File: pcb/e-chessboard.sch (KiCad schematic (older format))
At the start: 58 parts

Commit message: feat(kicad): adding ldr sensors
Adding ldr sensors to the matrix for checking the location of the chess
pieces.
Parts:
- removed D? (x9): D, Diode_SMD:D_SMA, symbol Device:D
- removed J?: e-magnet-2, lib_fp:20_15_electromagnet, symbol Connector:Conn_01x02_Male
- removed J?: e-magnet-5, lib_fp:20_15_electromagnet, symbol Connector:Conn_01x02_Male
- removed J?: e-magnet-8, lib_fp:20_15_electromagnet, symbol Connector:Conn_01x02_Male
- removed J?: e-magnet-4, lib_fp:20_15_electromagnet, symbol Connector:Conn_01x02_Male
- removed J?: e-magnet-1, lib_fp:20_15_electromagnet, symbol Connector:Conn_01x02_Male
- removed J?: e-magnet-3, lib_fp:20_15_electromagnet, symbol Connector:Conn_01x02_Male
- removed J?: e-magnet-7, lib_fp:20_15_electromagnet, symbol Connector:Conn_01x02_Male
- removed J?: e-magnet-6, lib_fp:20_15_electromagnet, symbol Connector:Conn_01x02_Male
- removed J?: e-magnet-9, lib_fp:20_15_electromagnet, symbol Connector:Conn_01x02_Male
- removed R? (x4): 100k, Resistor_SMD:R_0805_2012Metric, symbol Device:R
- added C?: 100nF, Capacitor_SMD:C_0805_2012Metric_Pad1.15x1.40mm_HandSolder, symbol Device:C
- added C?: 100n, Capacitor_SMD:C_0805_2012Metric_Pad1.15x1.40mm_HandSolder, symbol Device:C
- added D? (x9): D, Diode_SMD:D_SMA, symbol Device:D
- added D? (x6): D_Zener, Diode_SMD:D_SOD-110, symbol Device:D_Zener
- added R? (x3): 10k, Resistor_SMD:R_0805_2012Metric, symbol Device:R
- added U? (x9): MAGNET_LDR, lib_fp:20_15_electromagnet_ldr, symbol lib:MAGNET_LDR
- added U?: NCV7608, Package_SO:SOIC-28W_7.5x17.9mm_P1.27mm, symbol lib:NCV7608
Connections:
- net +12V: now also C?.2, U?.1 (D2), U?.24 (VS), U?.28 (D3), U?.4 (D1)
- net +3V3: now also C?.2, D?.1 (K), D?.1 (K), D?.1 (K), U?.8 (VCC)
- net GND: now also C?.1, C?.1, D?.2 (A), D?.2 (A), D?.2 (A), U?.10 (GND), U?.4, U?.4, U?.4, U?.4, U?.4, U?.4, U?.4, U?.4, U?.4
- net LDR_CS: now reaches U?.28 (IO17)
- net LDR_CS: now also U?.5 (CSB)
- net MAG_EN: now reaches U?.30 (IO18)
- net MAG_EN: now also U?.19 (EN)
- net LDR_EN: now reaches U?.31 (IO19)
- net LDR_EN: now also U?.19 (EN)
- net LDR_ADC3: now reaches U?.4 (SENSOR_VP)
- net LDR_ADC3: now also D?.1 (K), D?.2 (A), R?.2, U?.3, U?.3, U?.3
- net LDR_ADC1: now reaches U?.6 (IO34)
- net LDR_ADC1: now also D?.1 (K), D?.2 (A), R?.2, U?.3, U?.3, U?.3
- net LDR_ADC2: now reaches U?.7 (IO35)
- net LDR_ADC2: now also D?.1 (K), D?.2 (A), R?.2, U?.3, U?.3, U?.3
- net COL_1 renamed MAG_COL_1
- net MAG_COL_1: now also D?.1 (K), D?.1 (K), D?.1 (K), U?.2, U?.2, U?.2
- net COL_2 renamed MAG_COL_2
- net MAG_COL_2: now also D?.1 (K), D?.1 (K), D?.1 (K), U?.2, U?.2, U?.2
- net EN_MAG renamed MAG_CS
- net MAG_CS: now also U?.5 (CSB); no longer U?.19 (EN)
- net MISO_MAG renamed MISO
- net MISO: now also U?.9 (SO)
- net MOSI_MAG renamed MOSI
- net MOSI: now also U?.7 (SI)
- net PWM_ROW1 renamed MAG_PWM_ROW1
- net PWM_ROW2 renamed MAG_PWM_ROW2
- net PWM_ROW3 renamed MAG_PWM_ROW3
- net ROW_1 renamed MAG_ROW_1
- net MAG_ROW_1: now also D?.2 (A), D?.2 (A), D?.2 (A), U?.1, U?.1, U?.1
- net ROW_2 renamed MAG_ROW_2
- net MAG_ROW_2: now also D?.2 (A), D?.2 (A), D?.2 (A), U?.1, U?.1, U?.1
- net ROW_3 renamed MAG_ROW_3
- net MAG_ROW_3: now also D?.2 (A), D?.2 (A), D?.2 (A), U?.1, U?.1, U?.1
- net SCLK_MAG renamed SCLK
- net SCLK: now also U?.6 (SCLK)
- net SS_MAG: no longer names the net of U?.23 (IO15)
- net SS_MAG: no longer U?.5 (CSB)
- new net LDR_ROW1: R?.1, U?.3 (S1)
- new net LDR_ROW2: R?.1, U?.2 (S2)
- new net LDR_ROW3: R?.1, U?.27 (S3)
- new net MAG_COL_3: D?.1 (K), D?.1 (K), D?.1 (K), U?.2, U?.2, U?.2
- no-connect marks 30 -> 39
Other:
- moved on the sheet: C?, H?, J?, Q?, R?, SW?, U?

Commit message: feat(kicad): generating netlist
Fixing all erc issues, adding power and fuse footprints and generating
netlist.
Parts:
- F1: renamed from F?; footprint (none) -> Fuse:Fuseholder_Cylinder-5x20mm_Schurter_0031_8201_Horizontal_Open
- J1: renamed from J?; footprint (none) -> Connector_BarrelJack:BarrelJack_CUI_PJ-102AH_Horizontal
- gave numbers to parts that had none: 64
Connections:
- net COL_3 is gone; now on net MAG_COL_3: U3.27 (S3)
- net +3V3: now also C8.1, L1.2, R3.1

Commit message: fix(kicad): adding more traces
Adding traces and changing some schematic outputs for optimization.
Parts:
- R7, R8, R9: value 10k -> 300k
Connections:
- net LDR_ADC1: now also D1.2 (A), D2.1 (K), U1.4 (SENSOR_VP); no longer D6.2 (A), D7.1 (K), U1.6 (IO34)
- net LDR_ADC2: now also D6.2 (A), D7.1 (K), U1.6 (IO34); no longer D4.2 (A), D5.1 (K), U1.7 (IO35)
- net LDR_ADC3: now also D4.2 (A), D5.1 (K), U1.7 (IO35); no longer D1.2 (A), D2.1 (K), U1.4 (SENSOR_VP)
- net MAG_COL_1: now also D15.1 (K), D16.1 (K), D17.1 (K), U10.2, U11.2, U12.2; no longer D10.1 (K), D11.1 (K), D9.1 (K), U4.2, U5.2, U6.2
- net MAG_COL_3: now also D10.1 (K), D11.1 (K), D9.1 (K), U4.2, U5.2, U6.2; no longer D15.1 (K), D16.1 (K), D17.1 (K), U10.2, U11.2, U12.2
- net MAG_PWM_ROW1: now also U1.8 (IO32); no longer U1.12 (IO27)
- net MAG_PWM_ROW2: now also U1.9 (IO33); no longer U1.8 (IO32)
- net MAG_PWM_ROW3: now also U1.12 (IO27); no longer U1.9 (IO33)
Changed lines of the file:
@@
 Text GLabel 12750 4950 1    50   Input ~ 0
 MAG_COL_2
-Text GLabel 13750 4950 1    50   Input ~ 0
+Text GLabel 11750 5000 1    50   Input ~ 0
 MAG_COL_3
 $Comp
@@
 Text GLabel 9600 2150 2    50   Input ~ 0
 MAG_PWM_ROW3
+Text GLabel 2800 6500 2    50   Output ~ 0
+MAG_PWM_ROW1
+Text GLabel 2800 6600 2    50   Output ~ 0
+MAG_PWM_ROW2
 Text GLabel 2800 6400 2    50   Output ~ 0
-MAG_PWM_ROW1
-Text GLabel 2800 6500 2    50   Output ~ 0
-MAG_PWM_ROW2
-Text GLabel 2800 6600 2    50   Output ~ 0
 MAG_PWM_ROW3
 Text GLabel 9600 2450 2    50   Input ~ 0
@@
 Wire Wire Line
 	11750 5750 11600 5750
-Text GLabel 11750 5000 1    50   Input ~ 0
+Text GLabel 13750 4950 1    50   Input ~ 0
 MAG_COL_1
 Wire Wire Line
@@
 P 10350 5200
 F 0 "R7" V 10450 5150 50  0000 L CNN
-F 1 "10k" V 10350 5150 50  0000 L CNN
+F 1 "300k" V 10350 5100 50  0000 L CNN
 F 2 "Resistor_SMD:R_0805_2012Metric" V 10280 5200 50  0001 C CNN
 F 3 "~" H 10350 5200 50  0001 C CNN
@@
 P 10350 6200
 F 0 "R8" V 10450 6150 50  0000 L CNN
-F 1 "10k" V 10350 6150 50  0000 L CNN
+F 1 "300k" V 10350 6100 50  0000 L CNN
 F 2 "Resistor_SMD:R_0805_2012Metric" V 10280 6200 50  0001 C CNN
 F 3 "~" H 10350 6200 50  0001 C CNN
@@
 P 10350 7200
 F 0 "R9" V 10450 7150 50  0000 L CNN
-F 1 "10k" V 10350 7100 50  0000 L CNN
+F 1 "300k" V 10350 7100 50  0000 L CNN
 F 2 "Resistor_SMD:R_0805_2012Metric" V 10280 7200 50  0001 C CNN
 F 3 "~" H 10350 7200 50  0001 C CNN
@@
 Wire Wire Line
 	10550 5200 10550 5350
+Text GLabel 1050 4700 0    50   Input ~ 0
+LDR_ADC1
 Text GLabel 3500 7600 3    50   Input ~ 0
-LDR_ADC1
+LDR_ADC2
 Text GLabel 2800 7600 3    50   Input ~ 0
-LDR_ADC2
-Text GLabel 1050 4700 0    50   Input ~ 0
 LDR_ADC3
 $Comp

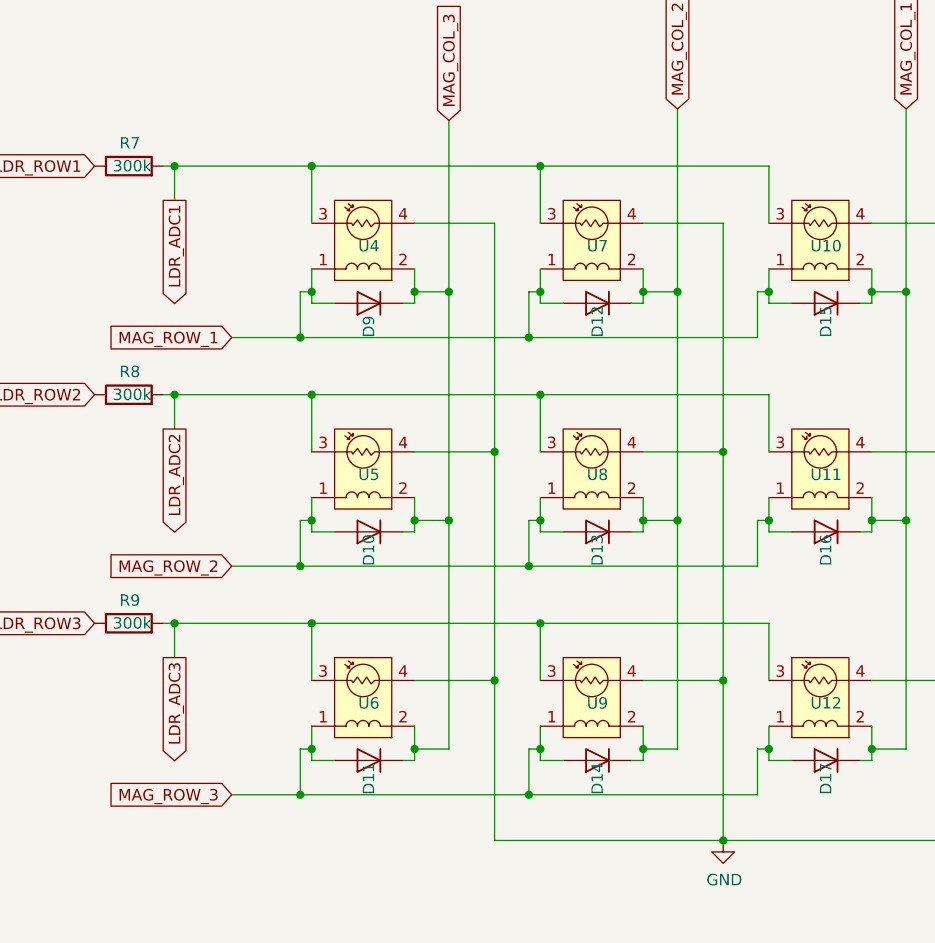
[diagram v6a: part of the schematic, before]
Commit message: fix(kicad): fixing wrong ldr lineup in the matrix
Fixing issue #2. Pcb not updated yet.
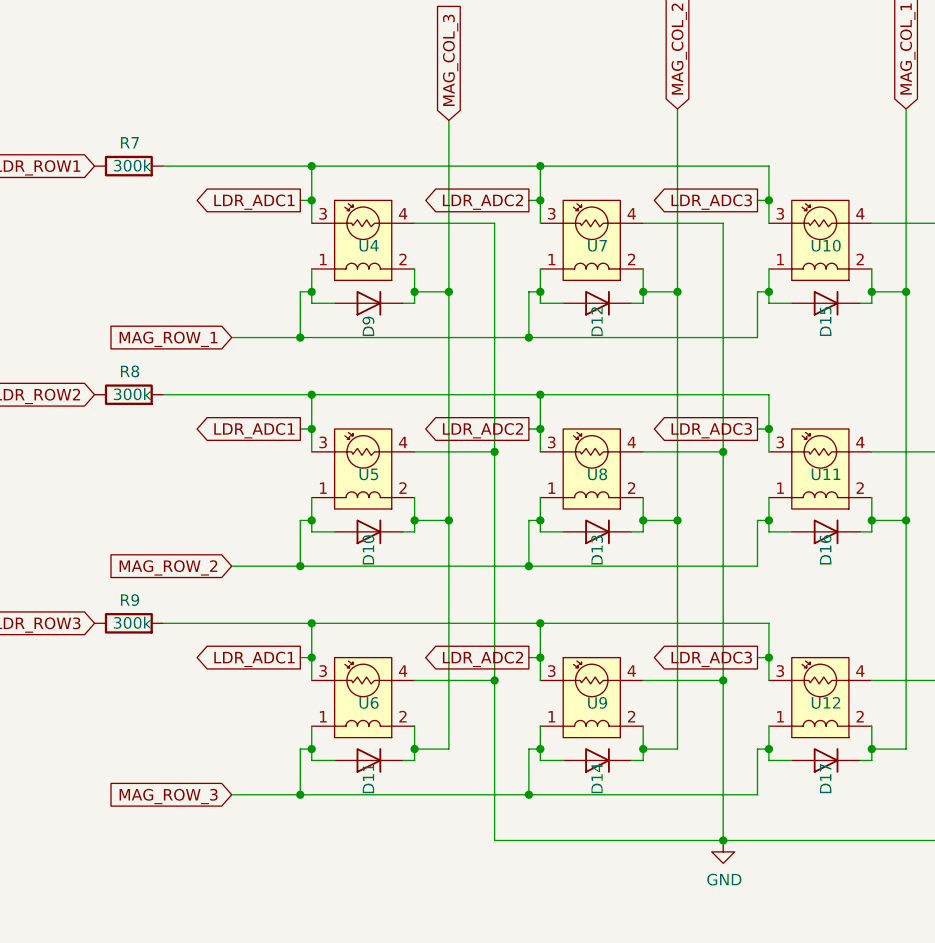
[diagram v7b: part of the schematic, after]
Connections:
- net LDR_ADC2 is gone; now on net LDR_ADC1: D6.2 (A), D7.1 (K), R8.2, U1.6 (IO34), U11.3, U5.3, U8.3
- net LDR_ADC3 is gone; now on net LDR_ADC1: D4.2 (A), D5.1 (K), R9.2, U1.7 (IO35), U12.3, U6.3, U9.3
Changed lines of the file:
@@
 LDR_ROW1
 Wire Wire Line
-	13150 5200 13150 5450
-Wire Wire Line
-	12150 5450 12150 5200
+	13150 5200 13150 5350
+Wire Wire Line
+	12150 5450 12150 5350
 Connection ~ 12150 5200
 Wire Wire Line
 	12150 5200 13150 5200
 Wire Wire Line
-	11150 5450 11150 5200
+	11150 5450 11150 5350
 Wire Wire Line
 	11150 5200 12150 5200
 Wire Wire Line
-	13150 6200 13150 6450
-Wire Wire Line
-	12150 6450 12150 6200
+	13150 6200 13150 6350
+Wire Wire Line
+	12150 6450 12150 6350
 Connection ~ 12150 6200
 Wire Wire Line
 	12150 6200 13150 6200
 Wire Wire Line
-	11150 6450 11150 6200
+	11150 6450 11150 6350
 Wire Wire Line
 	11150 6200 12150 6200
 Wire Wire Line
-	13150 7200 13150 7450
-Wire Wire Line
-	12150 7450 12150 7200
+	13150 7200 13150 7350
+Wire Wire Line
+	12150 7450 12150 7350
 Connection ~ 12150 7200
 Wire Wire Line
 	12150 7200 13150 7200
 Wire Wire Line
-	11150 7450 11150 7200
+	11150 7450 11150 7350
 Wire Wire Line
 	11150 7200 12150 7200
@@
 Wire Wire Line
 	12950 8150 13950 8150
-Text GLabel 10550 5350 3    50   Output ~ 0
+Text GLabel 11100 5350 0    50   Output ~ 0
 LDR_ADC1
-Text GLabel 10550 6350 3    50   Output ~ 0
+Text GLabel 12100 5350 0    50   Output ~ 0
 LDR_ADC2
-Text GLabel 10550 7350 3    50   Output ~ 0
+Text GLabel 13100 5350 0    50   Output ~ 0
 LDR_ADC3
 $Comp
@@
 	11750 5000 11750 5750
 Connection ~ 11750 5750
-Wire Wire Line
-	10500 5200 10550 5200
 Connection ~ 11150 5200
-Connection ~ 10550 5200
-Wire Wire Line
-	10550 5200 11150 5200
-Wire Wire Line
-	10500 6200 10550 6200
-Wire Wire Line
-	10550 6200 10550 6350
-Wire Wire Line
-	10550 6200 11150 6200
-Connection ~ 10550 6200
 Connection ~ 11150 6200
-Wire Wire Line
-	10500 7200 10550 7200
-Wire Wire Line
-	10550 7200 10550 7350
-Wire Wire Line
-	10550 7200 11150 7200
-Connection ~ 10550 7200
 Connection ~ 11150 7200
-Wire Wire Line
-	10550 5200 10550 5350
 Text GLabel 1050 4700 0    50   Input ~ 0
 LDR_ADC1
@@
 	0    1    1    0
 $EndComp
+Wire Wire Line
+	10500 5200 11150 5200
+Wire Wire Line
+	11100 5350 11150 5350
+Connection ~ 11150 5350
+Wire Wire Line
+	11150 5350 11150 5200
+Wire Wire Line
+	10500 6200 11150 6200
+Wire Wire Line
+	10500 7200 11150 7200
+Wire Wire Line
+	12100 5350 12150 5350
+Connection ~ 12150 5350
+Wire Wire Line
+	12150 5350 12150 5200
+Wire Wire Line
+	13100 5350 13150 5350
+Connection ~ 13150 5350
+Wire Wire Line
+	13150 5350 13150 5450
+Text GLabel 11100 6350 0    50   Output ~ 0
+LDR_ADC1
+Text GLabel 11100 7350 0    50   Output ~ 0
+LDR_ADC1
+Text GLabel 12100 6350 0    50   Output ~ 0
+LDR_ADC2
+Text GLabel 12100 7350 0    50   Output ~ 0
+LDR_ADC2
+Text GLabel 13100 6350 0    50   Output ~ 0
+LDR_ADC3
+Text GLabel 13100 7350 0    50   Output ~ 0
+LDR_ADC3
+Wire Wire Line
+	12100 7350 12150 7350
+Connection ~ 12150 7350
+Wire Wire Line
+	12150 7350 12150 7200
+Wire Wire Line
+	12100 6350 12150 6350
+Connection ~ 12150 6350
+Wire Wire Line
+	12150 6350 12150 6200
+Wire Wire Line
+	11100 6350 11150 6350
+Connection ~ 11150 6350
+Wire Wire Line
+	11150 6350 11150 6200
+Wire Wire Line
+	11100 7350 11150 7350
+Connection ~ 11150 7350
+Wire Wire Line
+	11150 7350 11150 7200
+Wire Wire Line
+	13100 7350 13150 7350
+Connection ~ 13150 7350
+Wire Wire Line
+	13150 7350 13150 7450
+Wire Wire Line
+	13100 6350 13150 6350
+Connection ~ 13150 6350
+Wire Wire Line
+	13150 6350 13150 6450
 $EndSCHEMATC
